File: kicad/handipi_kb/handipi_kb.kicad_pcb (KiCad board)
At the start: 2 copper layers, 104.9 x 75.2 mm, 94 parts, among them J1 USB_Connector, J2 RESET, J3 BOOT, SW1 SW_Push_Dual, SW10 SW_Push_Dual, SW11 SW_Push_Dual, SW12 SW_Push_Dual, SW13 SW_Push_Dual, SW14 SW_Push_Dual, SW15 SW_Push_Dual, SW16 SW_Push_Dual, SW17 SW_Push_Dual, SW18 SW_Push_Dual, SW19 SW_Push_Dual, SW2 SW_Push_Dual, SW20 SW_Push_Dual, SW21 SW_Push_Dual, SW22 SW_Push_Dual, SW23 SW_Push_Dual, SW24 SW_Push_Dual, SW25 SW_Push_Dual, SW26 SW_Push_Dual, SW27 SW_Push_Dual, SW28 SW_Push_Dual, SW29 SW_Push_Dual, SW3 SW_Push_Dual, SW30 SW_Push_Dual, SW31 SW_Push_Dual, SW32 SW_Push_Dual, SW33 SW_Push_Dual, SW34 SW_Push_Dual, SW35 SW_Push_Dual, SW36 SW_Push_Dual, SW39 5-way_switch, SW4 SW_Push_Dual, SW5 SW_Push_Dual, SW6 SW_Push_Dual, SW7 SW_Push_Dual, SW8 SW_Push_Dual, SW9 SW_Push_Dual, U1 ATmega328-PU, Y1 16mhz

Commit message: Starting docs
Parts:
- added PCBLogo: PCBLogo, RSU_Graphics:bblabs_logo_sml, F.Cu at (111.3, 100.8)
- LOGO1: renamed from G***; value LOGO -> LOGO1
- moved LOGO1 41.3 mm to (127.0, 85.3)
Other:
- outline, holes or cut-outs redrawn
- net class Default removed
- board text added: "bsp"
- board text added: "del"
- board text added: "ent"
- board text added: "esc"
- board text added: "spc"
- board text added: "tab"

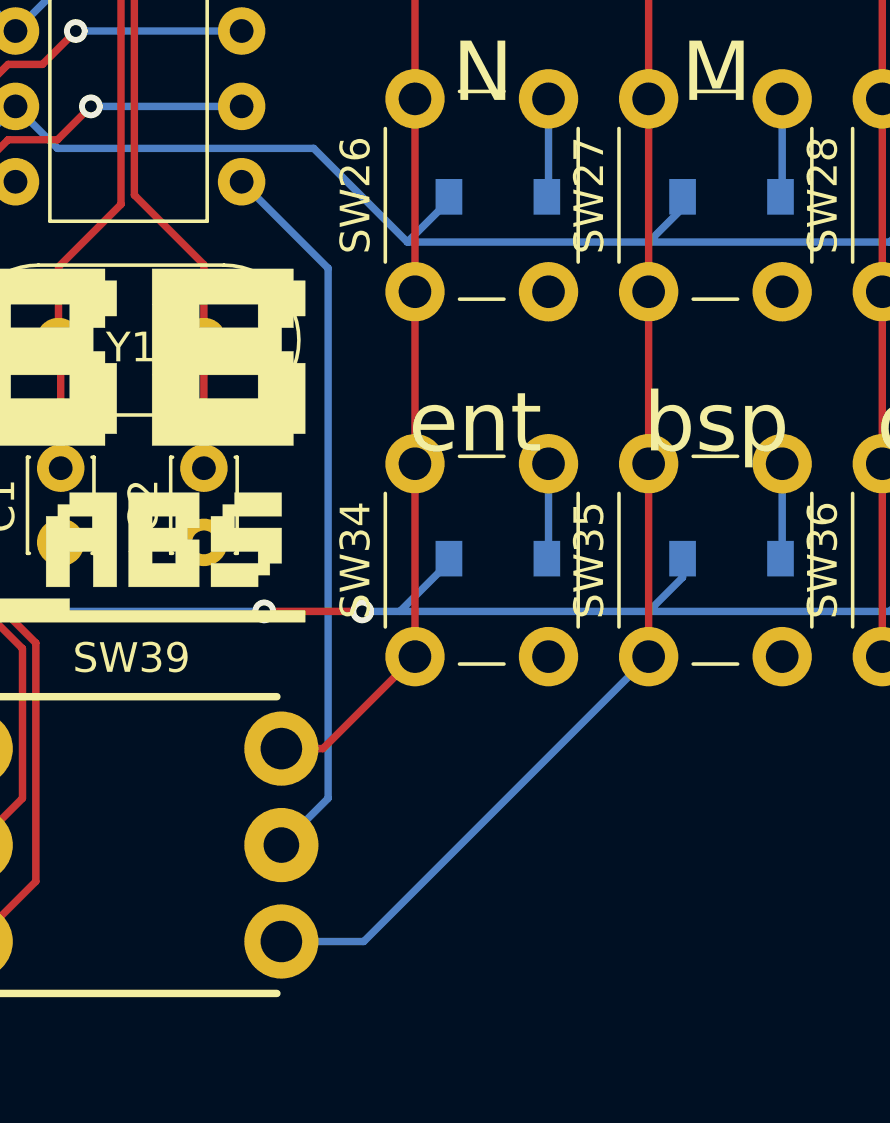
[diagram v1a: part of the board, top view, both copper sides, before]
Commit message: Fix footprint for directional switch
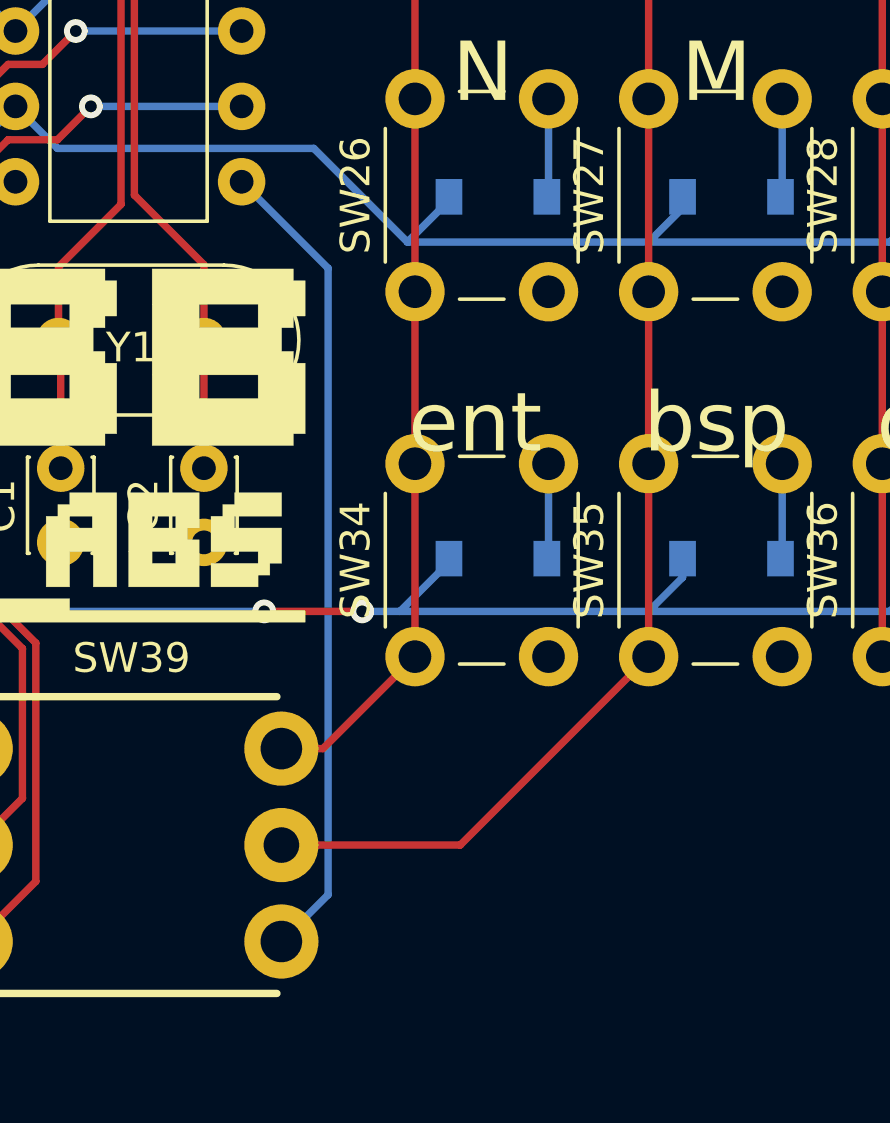
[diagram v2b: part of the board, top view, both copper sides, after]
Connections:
- H1 pad 1: Net-(H1-Pad1) -> unconnected-(H1-Pad1)
- H2 pad 1: Net-(H2-Pad1) -> unconnected-(H2-Pad1)
- H3 pad 1: Net-(H3-Pad1) -> unconnected-(H3-Pad1)
- H4 pad 1: Net-(H4-Pad1) -> unconnected-(H4-Pad1)
- SW39 pad 4: COL6 -> ROW4
- SW39 pad 5: ROW4 -> COL6
- U1 pad 18: Net-(U1-Pad18) -> unconnected-(U1-Pad18)
- U1 pad 19: Net-(U1-Pad19) -> unconnected-(U1-Pad19)
- U1 pad 21: Net-(U1-Pad21) -> unconnected-(U1-Pad21)
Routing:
- net ROW4: track 24.2 -> 27.5 mm
- net COL6: track 75.7 -> 74.3 mm

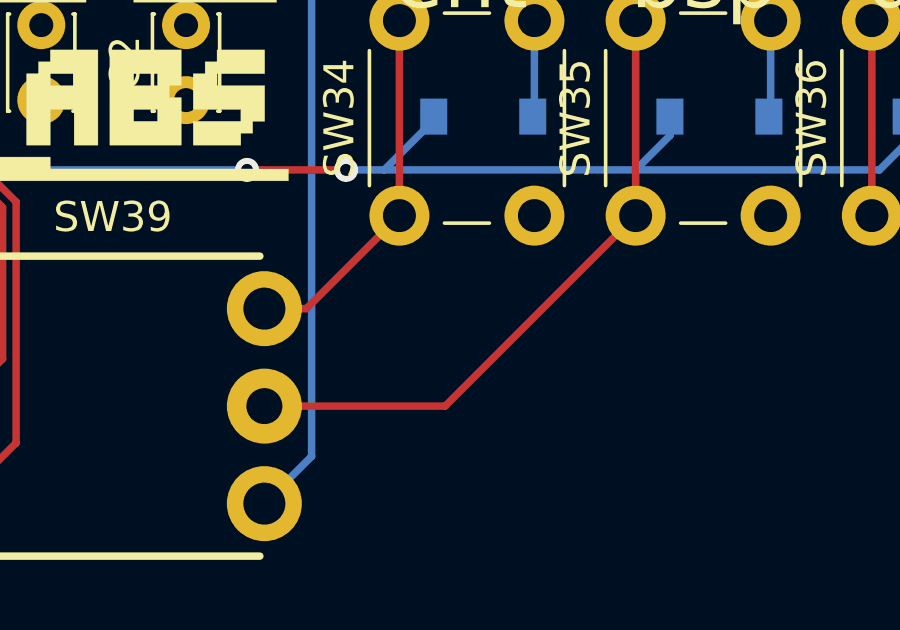
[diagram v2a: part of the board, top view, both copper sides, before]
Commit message: Fix ground connection for col 6
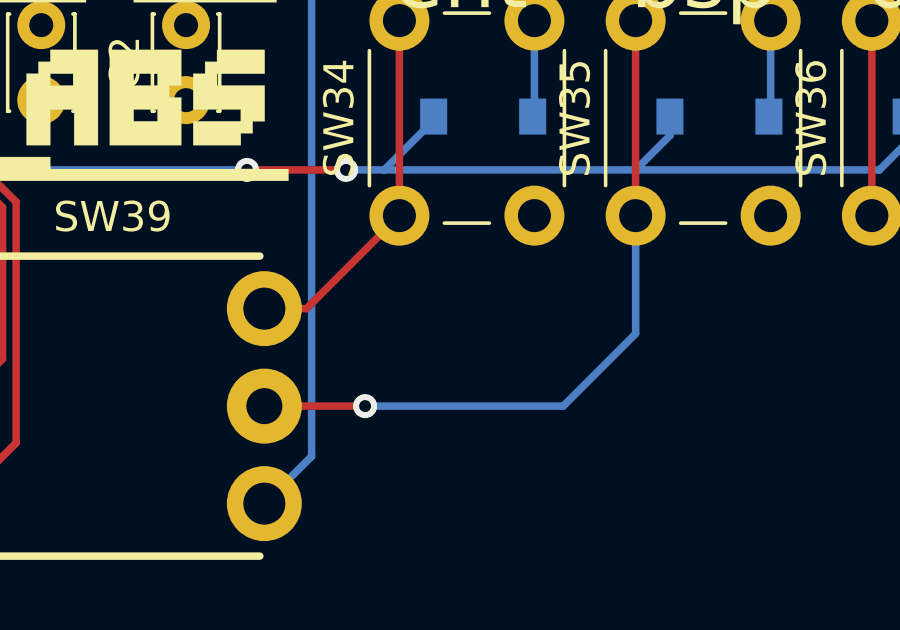
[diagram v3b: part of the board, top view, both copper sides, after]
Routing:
- net COL6: track 74.3 -> 76.6 mm, vias 0 -> 1
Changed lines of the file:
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@@
   (segment (start 136.652 48.872) (end 136.652 92.456) (width 0.25) (layer "F.Cu") (net 52))
   (segment (start 133.552 95.556) (end 132.15 95.556) (width 0.25) (layer "F.Cu") (net 52))
+  (segment (start 135.509 98.806) (end 132.15 98.806) (width 0.25) (layer "F.Cu") (net 53))
   (segment (start 134.317001 47.546999) (end 143.200999 47.546999) (width 0.25) (layer "F.Cu") (net 53))
-  (segment (start 144.526 92.456) (end 138.176 98.806) (width 0.25) (layer "F.Cu") (net 53))
   (segment (start 144.526 92.456) (end 144.526 48.872) (width 0.25) (layer "F.Cu") (net 53))
   (segment (start 143.200999 47.546999) (end 144.526 48.872) (width 0.25) (layer "F.Cu") (net 53))
   (segment (start 130.81 51.054) (end 134.317001 47.546999) (width 0.25) (layer "F.Cu") (net 53))
-  (segment (start 138.176 98.806) (end 132.15 98.806) (width 0.25) (layer "F.Cu") (net 53))
+  (via (at 135.509 98.806) (size 0.8) (drill 0.4) (layers "F.Cu" "B.Cu") (net 53))
+  (segment (start 144.526 96.393) (end 142.113 98.806) (width 0.25) (layer "B.Cu") (net 53))
+  (segment (start 144.526 92.456) (end 144.526 96.393) (width 0.25) (layer "B.Cu") (net 53))
+  (segment (start 142.113 98.806) (end 135.509 98.806) (width 0.25) (layer "B.Cu") (net 53))
   (segment (start 152.4 48.872) (end 152.4 92.456) (width 0.25) (layer "F.Cu") (net 54))
   (segment (start 150.624989 47.096989) (end 152.4 48.872) (width 0.25) (layer "F.Cu") (net 54))
@@
   (zone (net 1) (net_name "GND") (layer "F.Cu") (hatch edge 0.508)
     (connect_pads (clearance 0.508))
-    (min_thickness 0.254)
+    (min_thickness 0.254) (filled_areas_thickness no)
     (fill yes (thermal_gap 0.508) (thermal_bridge_width 0.508))
     (polygon
